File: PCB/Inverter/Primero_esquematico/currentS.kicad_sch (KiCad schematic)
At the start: 1 part, among them U18 HAH3DR 600-S0E

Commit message: Correcciones incompletas e instalaciones de un par de extensiones copadas
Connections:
- net 5V renamed +5V
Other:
- removed sheet SensorSuppy
- moved on the sheet: U18

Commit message: Termine el circuito de corriente
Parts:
- added J7: GT8E-5P-2H(55), Snapeda:HRS_GT8E-5P-2H_55_, symbol Snapeda:GT8E-5P-2H_55_
- U18: value HAH3DR 600-S0E -> HAH3DR 800-S07/SP4
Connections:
- net +5V: now also J7.1
- net GND: now also J7.2
- net Uot1: now also J7.3
- net Uot2: now also J7.4
- net Uot3: now also J7.5
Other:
- removed sheet FiltroSensor1
- removed sheet FiltroSensor2
- sheet FiltroSensor ports: added Sensor_In_1, Sensor_In_2, Sensor_In_3, Sensor_Out_1, Sensor_Out_2, Sensor_Out_3; removed Sensor_In, Sensor_Out
- note added: "Conector macho: https://www.digikey.com/en/products/detail/hirose-electric-co-ltd/GT8E-5S-HU/4305707"
- note added: "Conector para el: HAH3DR 600-S0E"
- note added: "Conector para el: HAH3DR 800-S07/SP4"
- note added: "Sensor de corriente: HAH3DR 600-S0E HAH3DR 800-S07/SP4"
- note added: "Son dos opciones similares y se lo va a hacer compatible para ambas por tema de disponibilidad"
- moved on the sheet: U18

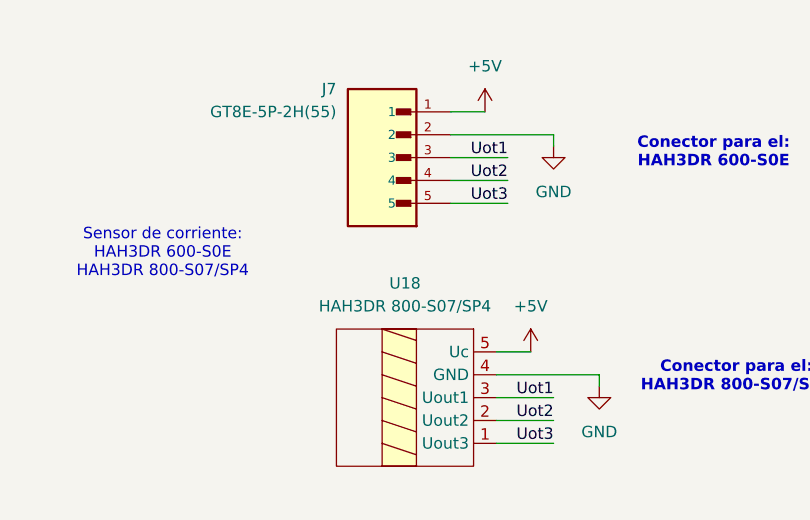
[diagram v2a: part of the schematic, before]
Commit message: Coloque filtros y sensores
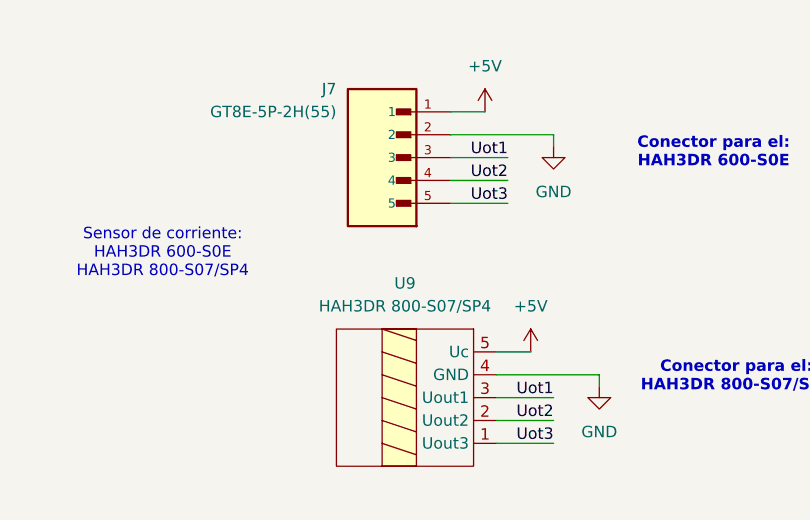
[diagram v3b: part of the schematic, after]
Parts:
- renumbered U18 to U9
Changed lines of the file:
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@@
 		(dnp no)
 		(fields_autoplaced yes)
-		(property "Reference" "#PWR098"
+		(property "Reference" "#PWR085"
 			(at 187.96 111.76 0)
 			(hide yes)
@@
 			(project "Primero_esquematico"
 				(path "/d930f486-f6ac-489c-907e-47f2cb34cf04/4b7a5665-e10a-4b94-9255-a8280a2a74a9"
-					(reference "#PWR098")
+					(reference "#PWR085")
 					(unit 1)
 				)
@@
 		(dnp no)
 		(fields_autoplaced yes)
-		(property "Reference" "#PWR0111"
+		(property "Reference" "#PWR084"
 			(at 182.88 85.09 0)
 			(hide yes)
@@
 			(project "Primero_esquematico"
 				(path "/d930f486-f6ac-489c-907e-47f2cb34cf04/4b7a5665-e10a-4b94-9255-a8280a2a74a9"
-					(reference "#PWR0111")
+					(reference "#PWR084")
 					(unit 1)
 				)
@@
 		(dnp no)
 		(fields_autoplaced yes)
-		(property "Reference" "#PWR064"
+		(property "Reference" "#PWR083"
 			(at 180.34 105.41 0)
 			(hide yes)
@@
 			(project "Primero_esquematico"
 				(path "/d930f486-f6ac-489c-907e-47f2cb34cf04/4b7a5665-e10a-4b94-9255-a8280a2a74a9"
-					(reference "#PWR064")
+					(reference "#PWR083")
 					(unit 1)
 				)
@@
 		(dnp no)
 		(fields_autoplaced yes)
-		(property "Reference" "U18"
+		(property "Reference" "U9"
 			(at 166.37 93.98 0)
 			(show_name no)
@@
 			(project "Primero_esquematico"
 				(path "/d930f486-f6ac-489c-907e-47f2cb34cf04/4b7a5665-e10a-4b94-9255-a8280a2a74a9"
-					(reference "U18")
+					(reference "U9")
 					(unit 1)
 				)
@@
 		(dnp no)
 		(fields_autoplaced yes)
-		(property "Reference" "#PWR079"
+		(property "Reference" "#PWR082"
 			(at 175.26 78.74 0)
 			(hide yes)
@@
 			(project "Primero_esquematico"
 				(path "/d930f486-f6ac-489c-907e-47f2cb34cf04/4b7a5665-e10a-4b94-9255-a8280a2a74a9"
-					(reference "#PWR079")
-					(unit 1)
-				)
+					(reference "#PWR082")
+					(unit 1)
+				)

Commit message: Esquematico practicamente terminado
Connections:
- net +5V renamed +5VA
- net GND renamed GND1

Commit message: Un par de cosas q corregi del ERC pero sigue mal
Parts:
- J7: footprint Snapeda:HRS_GT8E-5P-2H_55_ -> GT8E-5P-2H_55_:HRS_GT8E-5P-2H_55_
- U9: footprint (none) -> FSAE_footprints:HAH3DR 800-S07SP4
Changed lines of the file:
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@@
 			)
 		)
-		(property "Footprint" ""
+		(property "Footprint" "FSAE_footprints:HAH3DR 800-S07SP4"
 			(at 167.64 101.6 0)
 			(hide yes)
@@
 			)
 		)
-		(property "Footprint" "Snapeda:HRS_GT8E-5P-2H_55_"
+		(property "Footprint" "GT8E-5P-2H_55_:HRS_GT8E-5P-2H_55_"
 			(at 158.75 77.4699 0)
 			(hide yes)

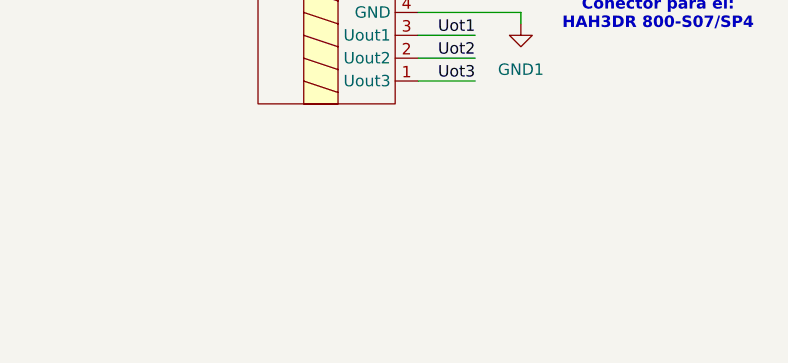
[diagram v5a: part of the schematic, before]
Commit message: Esquematico Listo
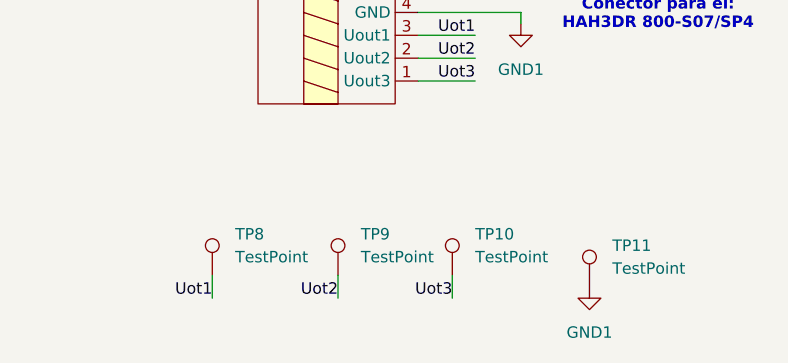
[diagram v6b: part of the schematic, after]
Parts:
- added TP10, TP11, TP8, TP9: TestPoint, TestPoint:TestPoint_Pad_D2.0mm, symbol Connector:TestPoint
- J7: footprint GT8E-5P-2H_55_:HRS_GT8E-5P-2H_55_ -> NuevoGui:HRS_GT8E-5P-2H_55_
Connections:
- net GND1: now also TP11.1
- net Uot1: now also TP8.1
- net Uot2: now also TP9.1
- net Uot3: now also TP10.1

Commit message: correcciones
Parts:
- TP37: renamed from TP8; footprint TestPoint:TestPoint_Pad_D2.0mm -> TestPoint:TestPoint_Pad_D1.0mm
- TP38: renamed from TP9; footprint TestPoint:TestPoint_Pad_D2.0mm -> TestPoint:TestPoint_Pad_D1.0mm
- TP39: renamed from TP10; footprint TestPoint:TestPoint_Pad_D2.0mm -> TestPoint:TestPoint_Pad_D1.0mm
- TP40: renamed from TP11; footprint TestPoint:TestPoint_Pad_D2.0mm -> TestPoint:TestPoint_Pad_D1.0mm
- renumbered J7 to J1, U9 to U31
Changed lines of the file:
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@@
 		(dnp no)
 		(fields_autoplaced yes)
-		(property "Reference" "#PWR0229"
+		(property "Reference" "#PWR0213"
 			(at 195.58 140.97 0)
 			(hide yes)
@@
 			(project "Primero_esquematico"
 				(path "/d930f486-f6ac-489c-907e-47f2cb34cf04/d101e913-ebd1-4e08-b728-82218f47123b/ea501642-1303-4ac1-bfff-b969418bd5d5"
-					(reference "#PWR0229")
+					(reference "#PWR0213")
 					(unit 1)
 				)
@@
 		(dnp no)
 		(fields_autoplaced yes)
-		(property "Reference" "TP11"
+		(property "Reference" "TP40"
 			(at 198.12 130.0479 0)
 			(show_name no)
@@
 			)
 		)
-		(property "Footprint" "TestPoint:TestPoint_Pad_D2.0mm"
+		(property "Footprint" "TestPoint:TestPoint_Pad_D1.0mm"
 			(at 200.66 134.62 0)
 			(hide yes)
@@
 			)
 		)
-		(pin "1"
-		)
-		(instances
-			(project "Primero_esquematico"
-				(path "/d930f486-f6ac-489c-907e-47f2cb34cf04/d101e913-ebd1-4e08-b728-82218f47123b/ea501642-1303-4ac1-bfff-b969418bd5d5"
-					(reference "TP11")
+		(property "Description_1" ""
+			(at 195.58 134.62 0)
+			(hide yes)
+			(show_name no)
+			(do_not_autoplace no)
+			(effects
+				(font
+					(size 1.27 1.27)
+				)
+			)
+		)
+		(pin "1"
+		)
+		(instances
+			(project "Primero_esquematico"
+				(path "/d930f486-f6ac-489c-907e-47f2cb34cf04/d101e913-ebd1-4e08-b728-82218f47123b/ea501642-1303-4ac1-bfff-b969418bd5d5"
+					(reference "TP40")
 					(unit 1)
 				)
@@
 		(dnp no)
 		(fields_autoplaced yes)
-		(property "Reference" "TP8"
+		(property "Reference" "TP37"
 			(at 156.21 128.7779 0)
 			(show_name no)
@@
 			)
 		)
-		(property "Footprint" "TestPoint:TestPoint_Pad_D2.0mm"
+		(property "Footprint" "TestPoint:TestPoint_Pad_D1.0mm"
 			(at 158.75 133.35 0)
 			(hide yes)
@@
 			)
 		)
-		(pin "1"
-		)
-		(instances
-			(project "Primero_esquematico"
-				(path "/d930f486-f6ac-489c-907e-47f2cb34cf04/d101e913-ebd1-4e08-b728-82218f47123b/ea501642-1303-4ac1-bfff-b969418bd5d5"
-					(reference "TP8")
+		(property "Description_1" ""
+			(at 153.67 133.35 0)
+			(hide yes)
+			(show_name no)
+			(do_not_autoplace no)
+			(effects
+				(font
+					(size 1.27 1.27)
+				)
+			)
+		)
+		(pin "1"
+		)
+		(instances
+			(project "Primero_esquematico"
+				(path "/d930f486-f6ac-489c-907e-47f2cb34cf04/d101e913-ebd1-4e08-b728-82218f47123b/ea501642-1303-4ac1-bfff-b969418bd5d5"
+					(reference "TP37")
 					(unit 1)
 				)
@@
 		(dnp no)
 		(fields_autoplaced yes)
-		(property "Reference" "#PWR01"
+		(property "Reference" "#PWR0210"
 			(at 181.61 105.41 0)
 			(hide yes)
@@
 			(project "Primero_esquematico"
 				(path "/d930f486-f6ac-489c-907e-47f2cb34cf04/d101e913-ebd1-4e08-b728-82218f47123b/ea501642-1303-4ac1-bfff-b969418bd5d5"
-					(reference "#PWR01")
+					(reference "#PWR0210")
 					(unit 1)
 				)
@@
 		(dnp no)
 		(fields_autoplaced yes)
-		(property "Reference" "#PWR010"
+		(property "Reference" "#PWR0209"
 			(at 175.26 78.74 0)
 			(hide yes)
@@
 			(project "Primero_esquematico"
 				(path "/d930f486-f6ac-489c-907e-47f2cb34cf04/d101e913-ebd1-4e08-b728-82218f47123b/ea501642-1303-4ac1-bfff-b969418bd5d5"
-					(reference "#PWR010")
+					(reference "#PWR0209")
 					(unit 1)
 				)
@@
 		(dnp no)
 		(fields_autoplaced yes)
-		(property "Reference" "#PWR084"
+		(property "Reference" "#PWR0211"
 			(at 182.88 85.09 0)
 			(hide yes)
@@
 			(project "Primero_esquematico"
 				(path "/d930f486-f6ac-489c-907e-47f2cb34cf04/d101e913-ebd1-4e08-b728-82218f47123b/ea501642-1303-4ac1-bfff-b969418bd5d5"
-					(reference "#PWR084")
+					(reference "#PWR0211")
 					(unit 1)
 				)
@@
 		(dnp no)
 		(fields_autoplaced yes)
-		(property "Reference" "#PWR085"
+		(property "Reference" "#PWR0212"
 			(at 187.96 111.76 0)
 			(hide yes)
@@
 			(project "Primero_esquematico"
 				(path "/d930f486-f6ac-489c-907e-47f2cb34cf04/d101e913-ebd1-4e08-b728-82218f47123b/ea501642-1303-4ac1-bfff-b969418bd5d5"
-					(reference "#PWR085")
+					(reference "#PWR0212")
 					(unit 1)
 				)
@@
 		(dnp no)
 		(fields_autoplaced yes)
-		(property "Reference" "U9"
+		(property "Reference" "U31"
 			(at 166.37 93.98 0)
 			(show_name no)
@@
 			)
 		)
+		(property "Description_1" ""
+			(at 168.91 101.6 0)
+			(hide yes)
+			(show_name no)
+			(do_not_autoplace no)
+			(effects
+				(font
+					(size 1.27 1.27)
+				)
+			)
+		)
 		(pin "5"
 		)
@@
 			(project "Primero_esquematico"
 				(path "/d930f486-f6ac-489c-907e-47f2cb34cf04/d101e913-ebd1-4e08-b728-82218f47123b/ea501642-1303-4ac1-bfff-b969418bd5d5"
-					(reference "U9")
+					(reference "U31")
 					(unit 1)
 				)
@@
 		(dnp no)
 		(fields_autoplaced yes)
-		(property "Reference" "TP9"
+		(property "Reference" "TP38"
 			(at 170.18 128.7779 0)
 			(show_name no)
@@
 			)
 		)
-		(property "Footprint" "TestPoint:TestPoint_Pad_D2.0mm"
+		(property "Footprint" "TestPoint:TestPoint_Pad_D1.0mm"
 			(at 172.72 133.35 0)
 			(hide yes)
@@
 			)
 		)
-		(pin "1"
-		)
-		(instances
-			(project "Primero_esquematico"
-				(path "/d930f486-f6ac-489c-907e-47f2cb34cf04/d101e913-ebd1-4e08-b728-82218f47123b/ea501642-1303-4ac1-bfff-b969418bd5d5"
-					(reference "TP9")
+		(property "Description_1" ""
+			(at 167.64 133.35 0)
+			(hide yes)
+			(show_name no)
+			(do_not_autoplace no)
+			(effects
+				(font
+					(size 1.27 1.27)
+				)
+			)
+		)
+		(pin "1"
+		)
+		(instances
+			(project "Primero_esquematico"
+				(path "/d930f486-f6ac-489c-907e-47f2cb34cf04/d101e913-ebd1-4e08-b728-82218f47123b/ea501642-1303-4ac1-bfff-b969418bd5d5"
+					(reference "TP38")
 					(unit 1)
 				)
@@
 		(in_pos_files yes)
 		(dnp no)
-		(property "Reference" "J7"
+		(property "Reference" "J1"
 			(at 158.75 72.3899 0)
 			(show_name no)
@@
 			)
 		)
+		(property "Description_1" ""
+			(at 163.83 80.01 0)
+			(hide yes)
+			(show_name no)
+			(do_not_autoplace no)
+			(effects
+				(font
+					(size 1.27 1.27)
+				)
+			)
+		)
 		(pin "4"
 		)
@@
 			(project "Primero_esquematico"
 				(path "/d930f486-f6ac-489c-907e-47f2cb34cf04/d101e913-ebd1-4e08-b728-82218f47123b/ea501642-1303-4ac1-bfff-b969418bd5d5"
-					(reference "J7")
+					(reference "J1")
 					(unit 1)
 				)
@@
 		(dnp no)
 		(fields_autoplaced yes)
-		(property "Reference" "TP10"
+		(property "Reference" "TP39"
 			(at 182.88 128.7779 0)
 			(show_name no)
@@
 			)
 		)
-		(property "Footprint" "TestPoint:TestPoint_Pad_D2.0mm"
+		(property "Footprint" "TestPoint:TestPoint_Pad_D1.0mm"
 			(at 185.42 133.35 0)
 			(hide yes)
@@
 			)
 		)
-		(pin "1"
-		)
-		(instances
-			(project "Primero_esquematico"
-				(path "/d930f486-f6ac-489c-907e-47f2cb34cf04/d101e913-ebd1-4e08-b728-82218f47123b/ea501642-1303-4ac1-bfff-b969418bd5d5"
-					(reference "TP10")
-					(unit 1)
-				)
+		(property "Description_1" ""
+			(at 180.34 133.35 0)
+			(hide yes)
+			(show_name no)
+			(do_not_autoplace no)
+			(effects
+				(font
+					(size 1.27 1.27)
+				)
+			)
+		)
+		(pin "1"
+		)
+		(instances
+			(project "Primero_esquematico"
+				(path "/d930f486-f6ac-489c-907e-47f2cb34cf04/d101e913-ebd1-4e08-b728-82218f47123b/ea501642-1303-4ac1-bfff-b969418bd5d5"
+					(reference "TP39")
+					(unit 1)
+				)

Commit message: Corregi cosas de la placa
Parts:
- renumbered J1 to J2, U31 to U30
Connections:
- net +5VA renamed +5V
- net GND1 renamed GND
